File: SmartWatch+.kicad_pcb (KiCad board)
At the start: 2 copper layers, 62.7 x 32.2 mm, 6 parts, among them IC1 DS1315-5+, J1 2-1571586-9, J2 2-1571586-9

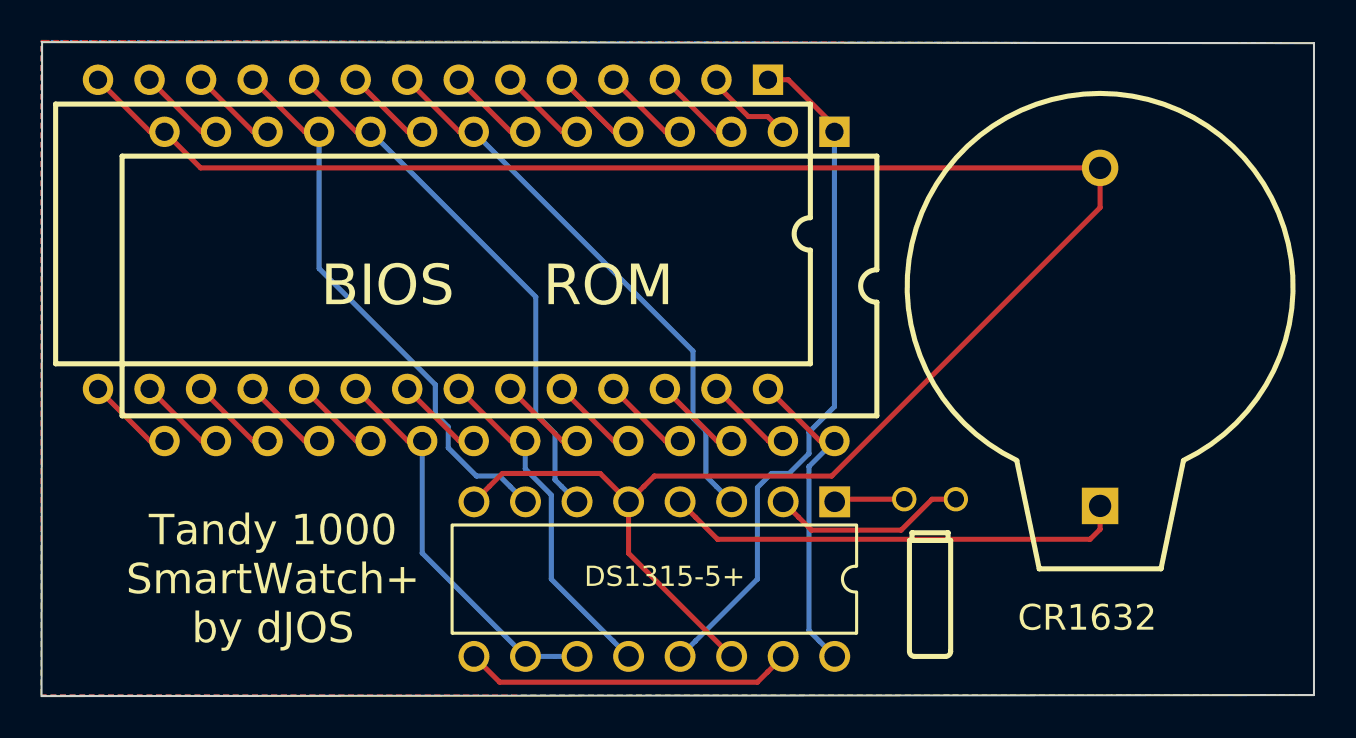
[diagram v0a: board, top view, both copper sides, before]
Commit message: Add files via upload
Updated 28-pin Socket to have actual Pin Lables.
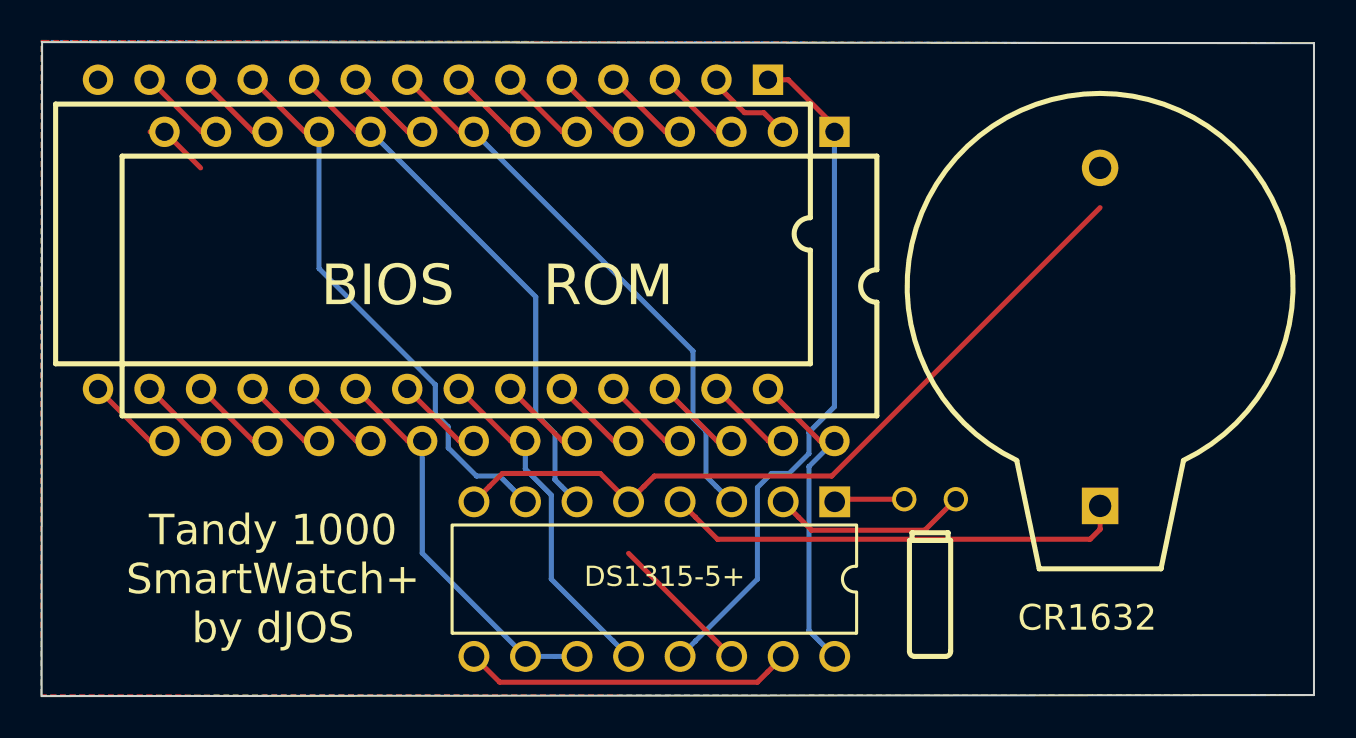
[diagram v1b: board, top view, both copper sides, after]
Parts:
- removed 3.768kHz1: Crystal Oscillator, Dereks Parts:TC26H
- removed G***: LOGO, Symbol:HHGTTG_Logo
- added XO1: 32.7680Khz, Dereks_Parts:TC26H, F.Cu at (64.4, 43.1)
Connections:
- net /A15 renamed /D3
- net /A16 renamed /D4
- net /A17 renamed /D5
- net /A18 renamed /D6
- net /A19 renamed /D7
- net /A20 renamed /CE
- net /A22 renamed /OE
- net /A27 renamed /A14
- net /A28 renamed /VCC
- IC1 pad 13: /A1 -> /VPP
- IC1 pad 3: /A8 -> /A2
- IC1 pad 6: /A10 -> /A0
- IC1 pad 7: /A11 -> /D0
- J1 pad 1: /A1 -> /VPP
- J1 pad 10: /A10 -> /A0
- J1 pad 11: /A11 -> /D0
- J1 pad 12: /A12 -> /D1
- J1 pad 13: /A13 -> /D2
- J1 pad 2: /A2 -> /A12
- J1 pad 21: /A21 -> /A10
- J1 pad 23: /A23 -> /A11
- J1 pad 24: /A24 -> /A9
- J1 pad 25: /A25 -> /A8
- J1 pad 26: /A26 -> /A13
- J1 pad 3: /A3 -> /A7
- J1 pad 4: /A4 -> /A6
- J1 pad 6: /A6 -> /A4
- J1 pad 7: /A7 -> /A3
- J1 pad 8: /A8 -> /A2
- J1 pad 9: /A9 -> /A1
- J2 pad 1: /A1 -> /VPP
- J2 pad 10: /A10 -> /A0
- J2 pad 11: /A11 -> /D0
- J2 pad 12: /A12 -> /D1
- J2 pad 13: /A13 -> /D2
- J2 pad 2: /A2 -> /A12
- J2 pad 21: /A21 -> /A10
- J2 pad 23: /A23 -> /A11
- J2 pad 24: /A24 -> /A9
- J2 pad 25: /A25 -> /A8
- J2 pad 26: /A26 -> /A13
- J2 pad 3: /A3 -> /A7
- J2 pad 4: /A4 -> /A6
- J2 pad 6: /A6 -> /A4
- J2 pad 7: /A7 -> /A3
- J2 pad 8: /A8 -> /A2
- J2 pad 9: /A9 -> /A1
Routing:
- net GND: track 100.9 -> 48.4 mm
- net /VPP: track 0.00 -> 34.0 mm
- net /A1: track 34.0 -> 4.34 mm
- net /D0: track 0.00 -> 27.5 mm
- net /A0: track 0.00 -> 26.8 mm
- net /A8: track 27.8 -> 4.34 mm
- net /A2: track 4.48 -> 27.8 mm
- net /A11: track 27.5 -> 4.34 mm
- net /A10: track 26.8 -> 4.34 mm
- net /D1: track 0.00 -> 4.34 mm
- net /A24: track 4.34 -> 0.00 mm
- net /A23: track 4.34 -> 0.00 mm
- net /A21: track 4.34 -> 0.00 mm
- net /D2: track 0.00 -> 4.34 mm
- net /A26: track 4.34 -> 0.00 mm
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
